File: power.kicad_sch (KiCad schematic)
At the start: 21 parts, among them J1 USB_C_Receptacle_USB2.0_16P, J2 JST_SH_SM04B-SRSS-TB, J6 JST-SM02B-SRSS-TB, Q1 Si2301CDS, SW62 MSK-12C02, U2 USBLC6-2SC6, U3 TP4056, U4 XC6206PxxxMR

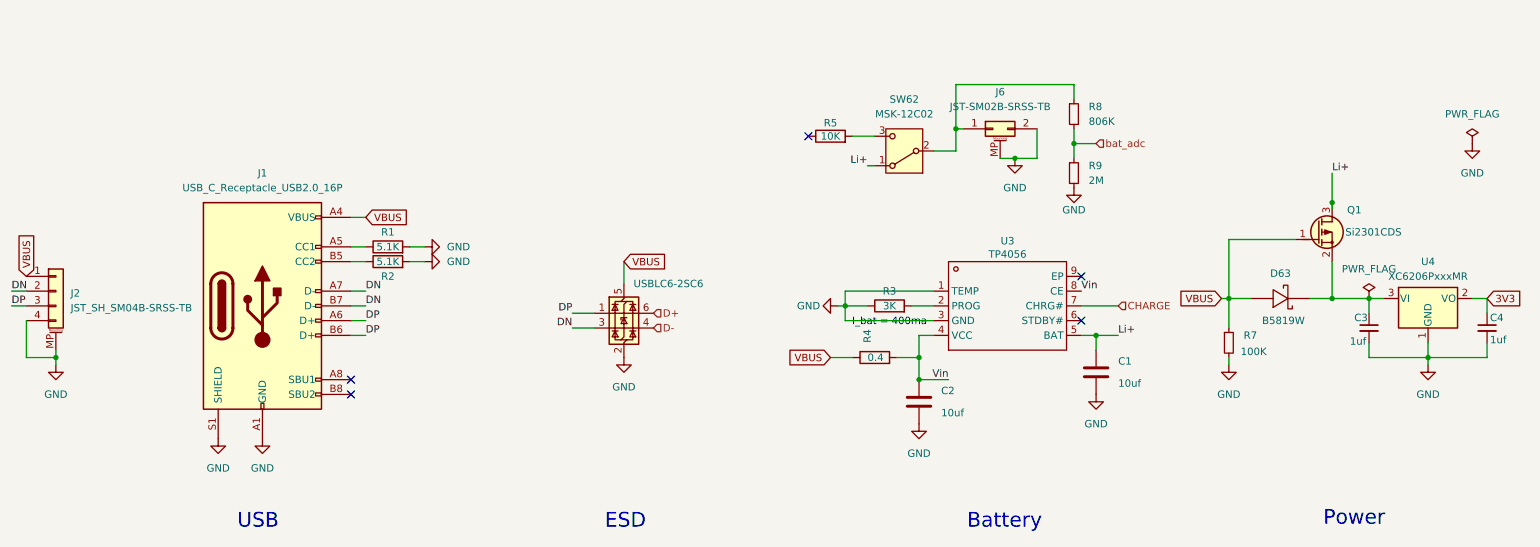
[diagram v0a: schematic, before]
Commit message: add rmk-ble-keyboard %65
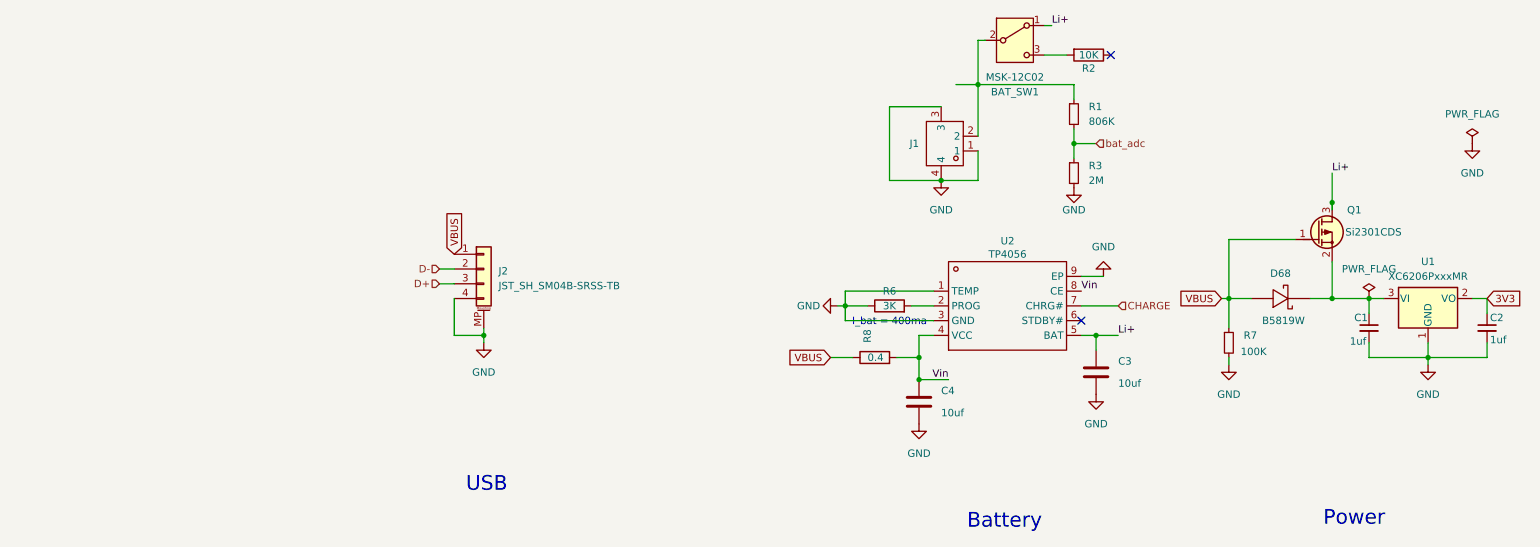
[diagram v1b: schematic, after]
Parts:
- removed J1: USB_C_Receptacle_USB2.0_16P, Connector_USB:USB_C_Receptacle_GCT_USB4105-xx-A_16P_TopMnt_Horizontal, symbol Connector:USB_C_Receptacle_USB2.0_16P
- removed J6: JST-SM02B-SRSS-TB, Connector_JST:JST_SH_SM02B-SRSS-TB_1x02-1MP_P1.00mm_Horizontal, symbol Connector_Generic_MountingPin:Conn_02x01_MountingPin
- removed R1, R2: 5.1K, Resistor_SMD:R_0603_1608Metric_Pad0.98x0.95mm_HandSolder, symbol Device:R
- removed U2: USBLC6-2SC6, Package_TO_SOT_SMD:SOT-23-6, symbol Power_Protection:USBLC6-2SC6
- added J1: ~, XY-MX1.25-2A71:CONN-SMD_2P-P1.25_XYECONN_XY-MX1.25-2A71, symbol XY-MX1.25-2A71:XY-MX1.25-2A71
- renumbered SW62 to BAT_SW1, C3 to C1, C4 to C2, C1 to C3, C2 to C4, D63 to D68, R8 to R1, R5 to R2, R9 to R3, R3 to R6, R4 to R8, U4 to U1, U3 to U2
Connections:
- net DN is gone; now on net D-: J2.2 (Pin_2)
- net DP is gone; now on net D+: J2.3 (Pin_3)
- net GND: now also U2.9 (EP), J1.1, J1.3, J1.4
- net at BAT_SW1.2 (B), R1.1: now also J1.2
- no-connect marks 5 -> 2
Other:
- note removed: "ESD"
- moved on the sheet: BAT_SW1, J2, R2

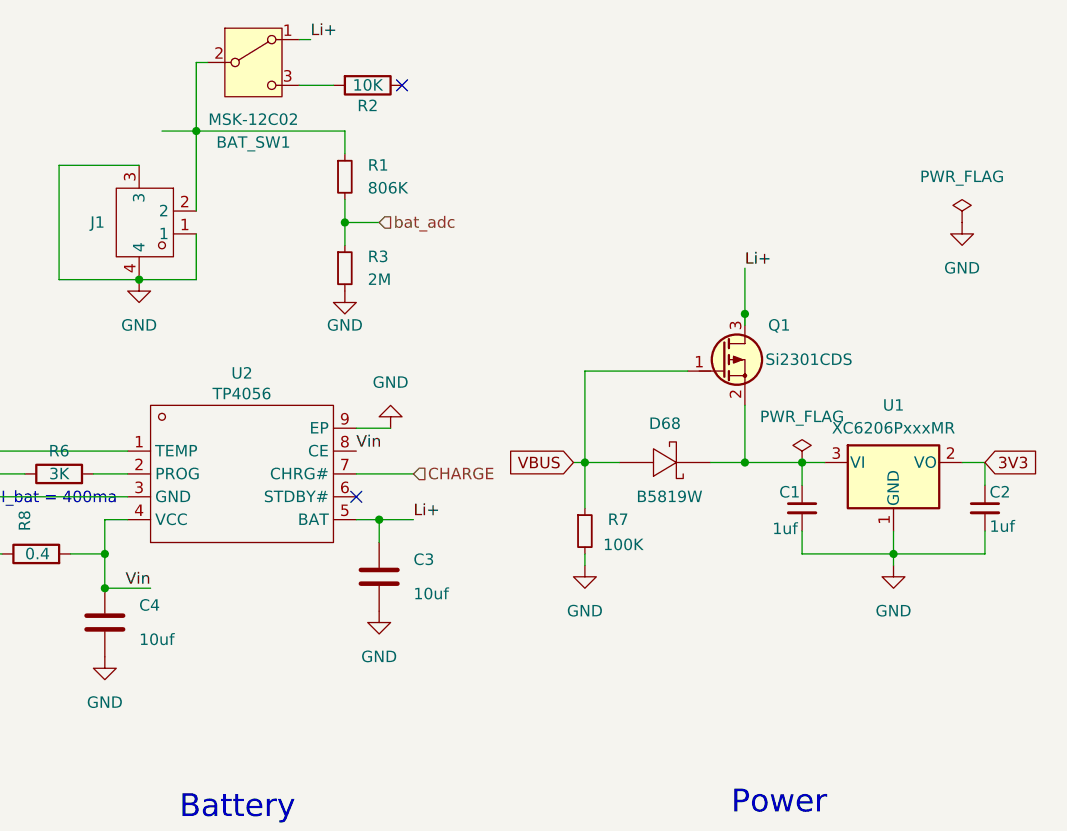
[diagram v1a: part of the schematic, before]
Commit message: update rmk-ble-keyboard %65
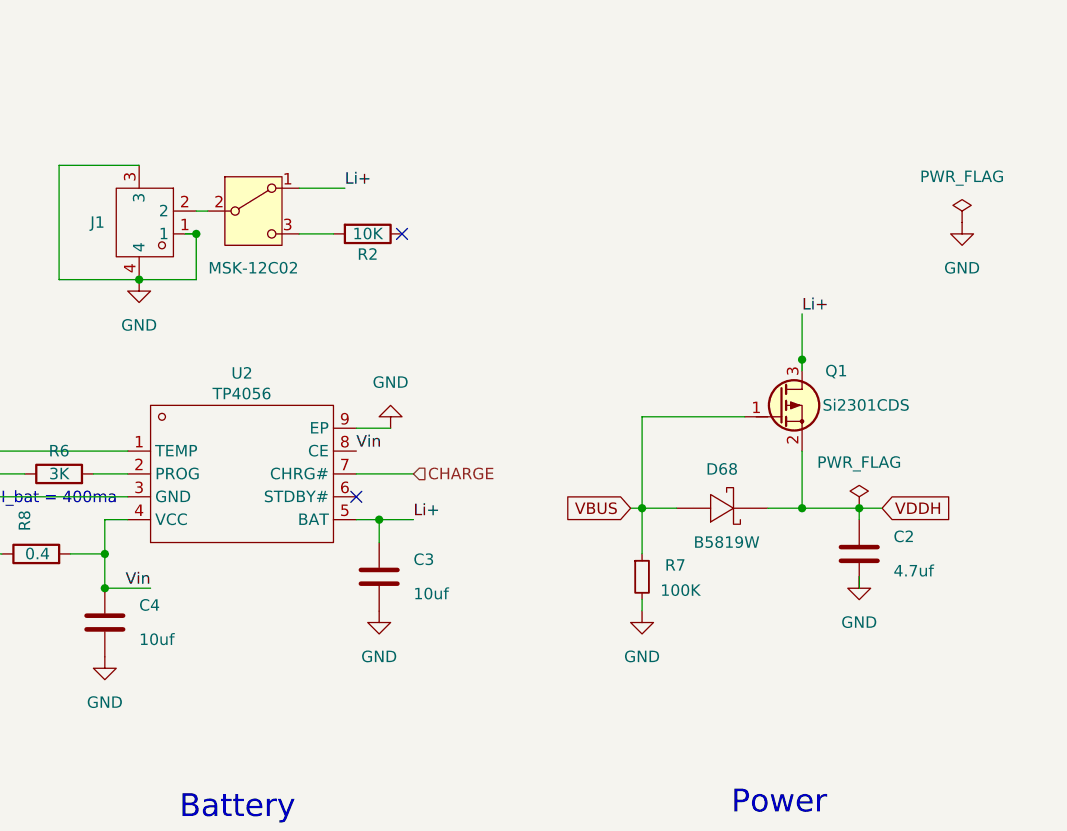
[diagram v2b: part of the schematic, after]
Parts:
- removed C1, C2: 1uf, Capacitor_SMD:C_0603_1608Metric_Pad1.08x0.95mm_HandSolder, symbol Device:C_Small
- removed R1: 806K, Resistor_SMD:R_0603_1608Metric_Pad0.98x0.95mm_HandSolder, symbol Device:R_Small
- removed R3: 2M, Resistor_SMD:R_0603_1608Metric_Pad0.98x0.95mm_HandSolder, symbol Device:R_Small
- removed U1: XC6206PxxxMR, Package_TO_SOT_SMD:SOT-23-3, symbol Regulator_Linear:XC6206PxxxMR
- added C2: 4.7uf, Capacitor_SMD:C_0603_1608Metric_Pad1.08x0.95mm_HandSolder, symbol Device:C
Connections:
- net GND: now also C2.2
- net VDDH: now reaches D68.1 (-), Q1.2 (S)
- net VDDH: now also C2.1
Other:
- moved on the sheet: D68, Q1, R2, R7
